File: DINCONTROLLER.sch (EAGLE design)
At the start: 44 parts, among them IC1 ESPWROOM32, SW1 TAC-SWITCH-LEDSP0620, SW2 TAC-SWITCH-LEDSP0620, SW3 TAC-SWITCH-LEDSP0620, SW4 TAC-SWITCH-LEDSP0620, SW5 TAC-SWITCH-LEDSP0620, SW6 TAC-SWITCH-LEDSP0620, SW7 TAC-SWITCH-LEDSP0620, SW8 TAC-SWITCH-LEDSP0620

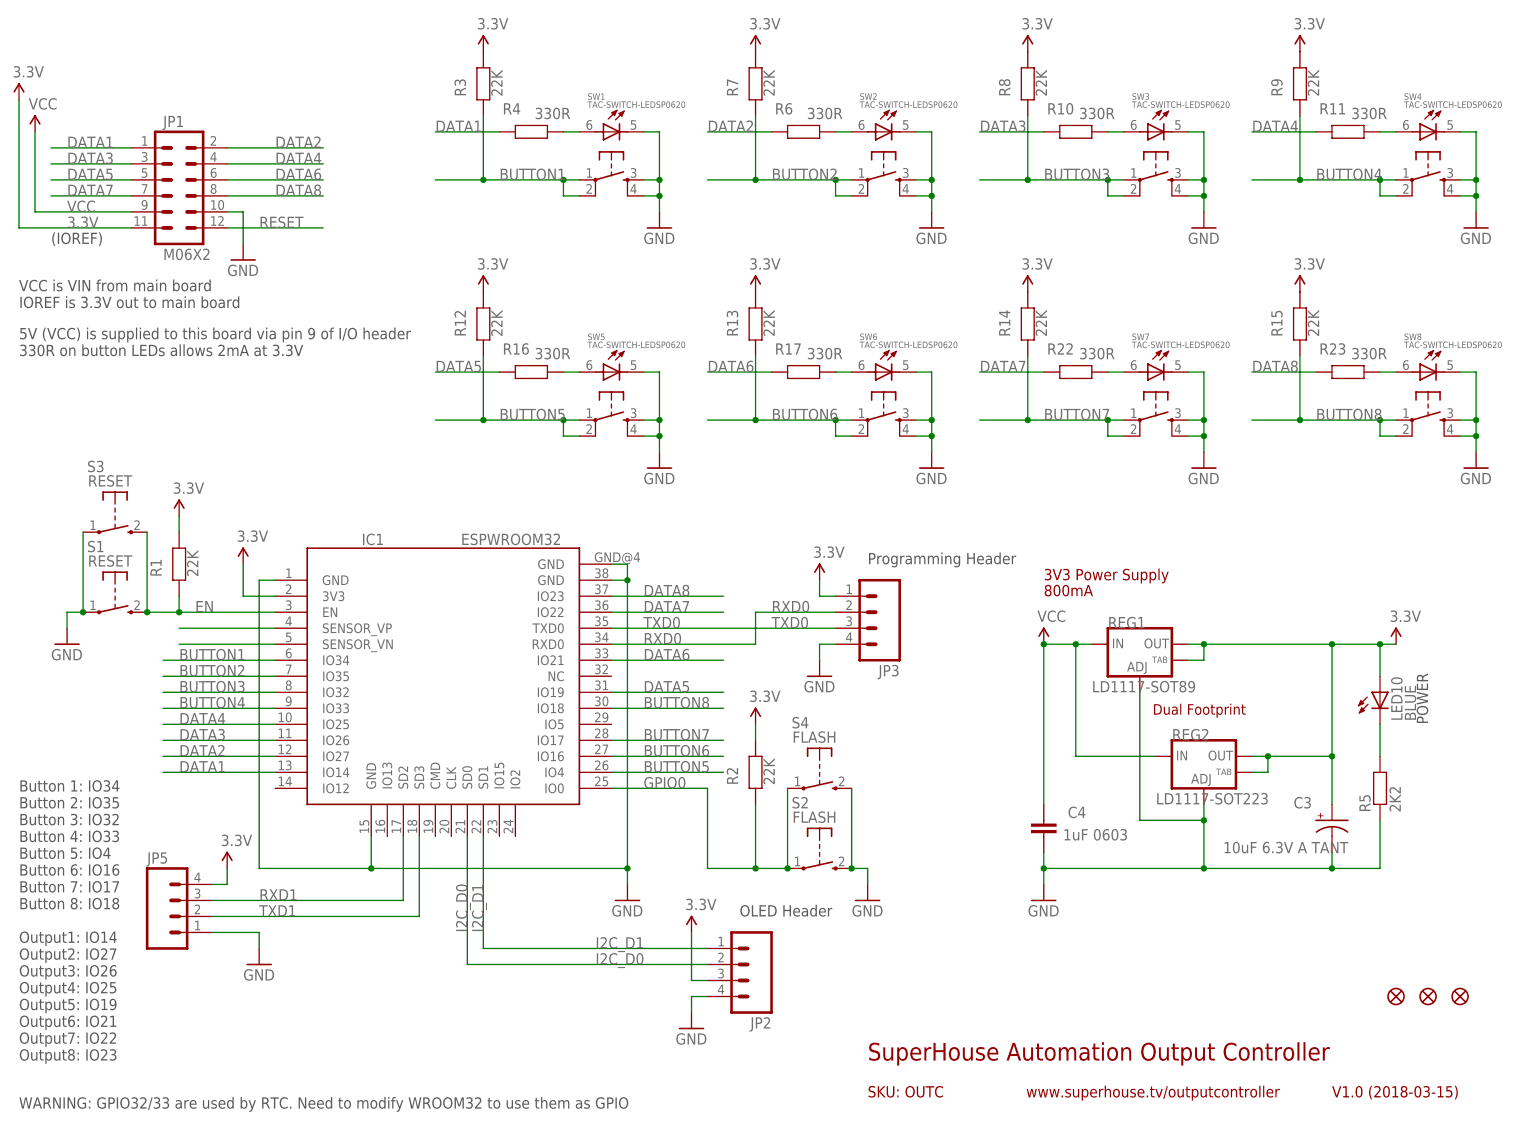
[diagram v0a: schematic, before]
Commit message: Improved designators
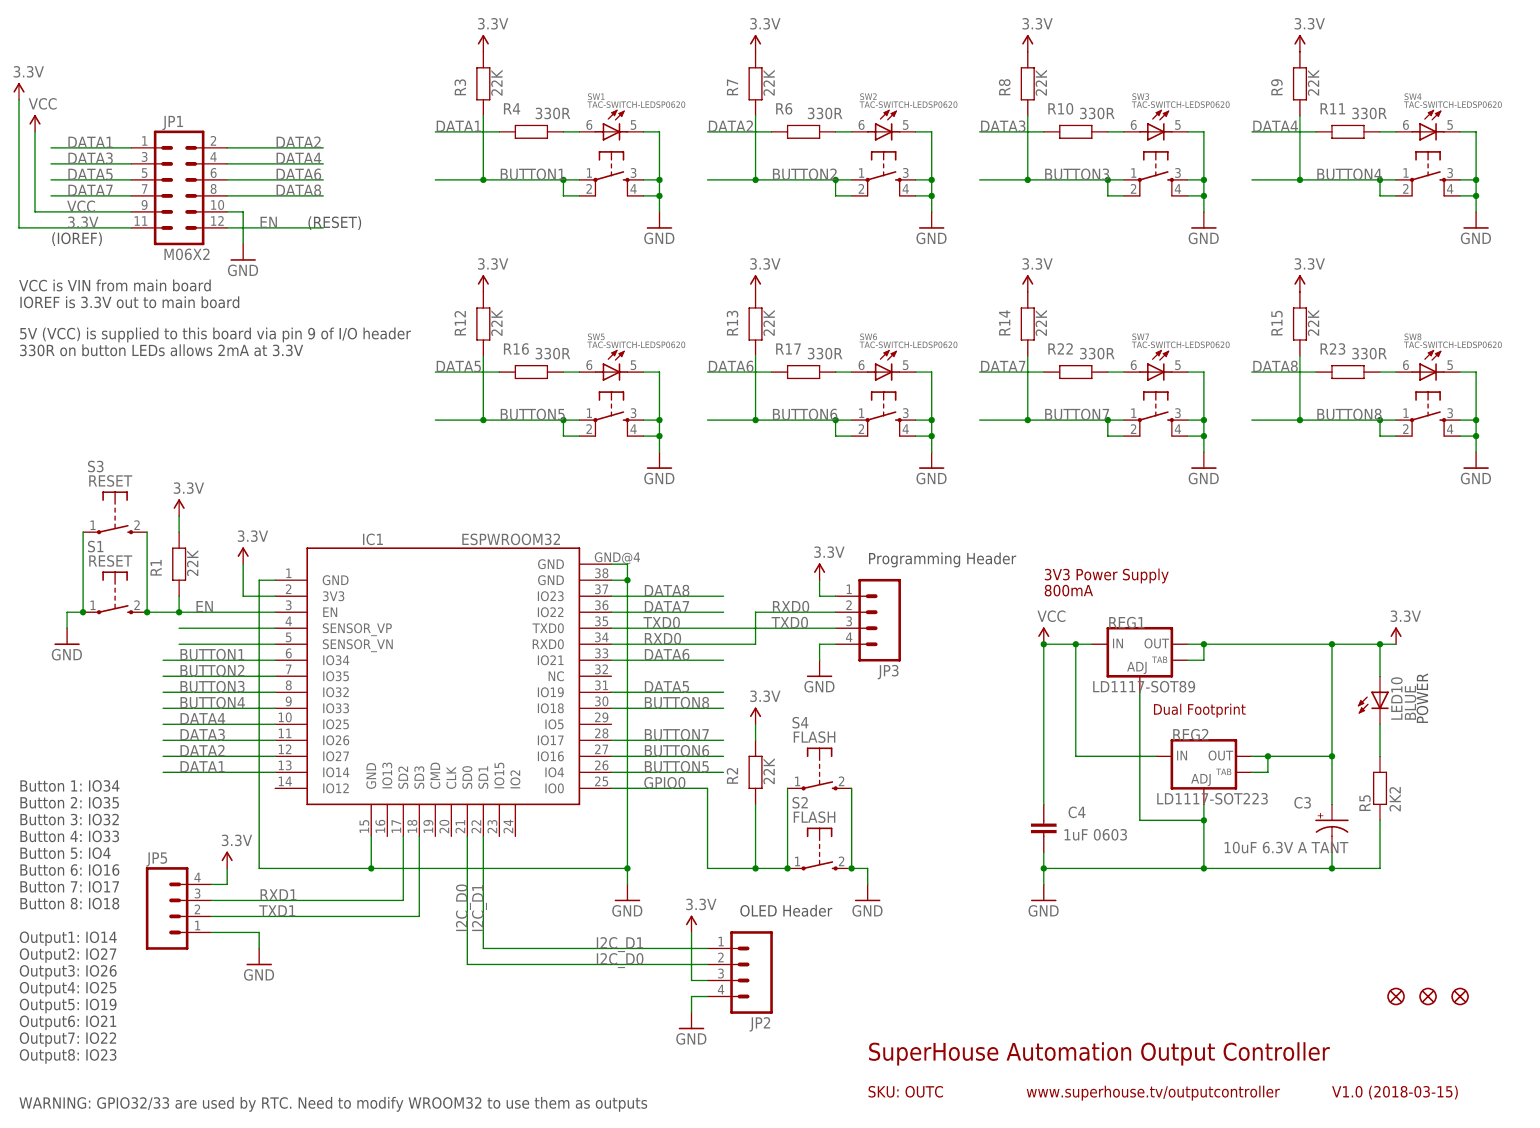
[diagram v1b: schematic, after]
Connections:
- removed net RESET: JP1.12
- net EN: now also JP1.12
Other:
- note added: "(RESET)"
- note added: "WARNING: GPIO32/33 are used by RTC. Need to modify WROOM32 to use them as outputs"
- note removed: "WARNING: GPIO32/33 are used by RTC. Need to modify WROOM32 to use them as GPIO"
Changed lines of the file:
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@@
 <text x="170.18" y="86.36" size="1.778" layer="94">800mA</text>
 <text x="12.7" y="142.24" size="1.778" layer="97">(IOREF)</text>
-<text x="7.62" y="5.08" size="1.778" layer="97">WARNING: GPIO32/33 are used by RTC. Need to modify WROOM32 to use them as GPIO</text>
+<text x="7.62" y="5.08" size="1.778" layer="97">WARNING: GPIO32/33 are used by RTC. Need to modify WROOM32 to use them as outputs</text>
 <text x="121.92" y="35.56" size="1.778" layer="97">OLED Header</text>
 <text x="142.24" y="91.44" size="1.778" layer="97">Programming Header</text>
+<text x="53.34" y="144.78" size="1.778" layer="97">(RESET)</text>
 </plain>
 <instances>
@@
 <label x="33.02" y="66.04" size="1.778" layer="95"/>
 <pinref part="IC1" gate="IC$1" pin="IO25"/>
-</segment>
-</net>
-<net name="RESET" class="0">
-<segment>
-<pinref part="JP1" gate="G$1" pin="12"/>
-<wire x1="40.64" y1="144.78" x2="55.88" y2="144.78" width="0.1524" layer="91"/>
-<label x="45.72" y="144.78" size="1.778" layer="95"/>
 </segment>
 </net>
@@
 <junction x="27.94" y="83.82"/>
 </segment>
+<segment>
+<pinref part="JP1" gate="G$1" pin="12"/>
+<wire x1="40.64" y1="144.78" x2="55.88" y2="144.78" width="0.1524" layer="91"/>
+<label x="45.72" y="144.78" size="1.778" layer="95"/>
+</segment>
 </net>
 <net name="GPIO0" class="0">
@@
 </sheet>
 </sheets>
+<errors>
+</errors>
 </schematic>
 </drawing>

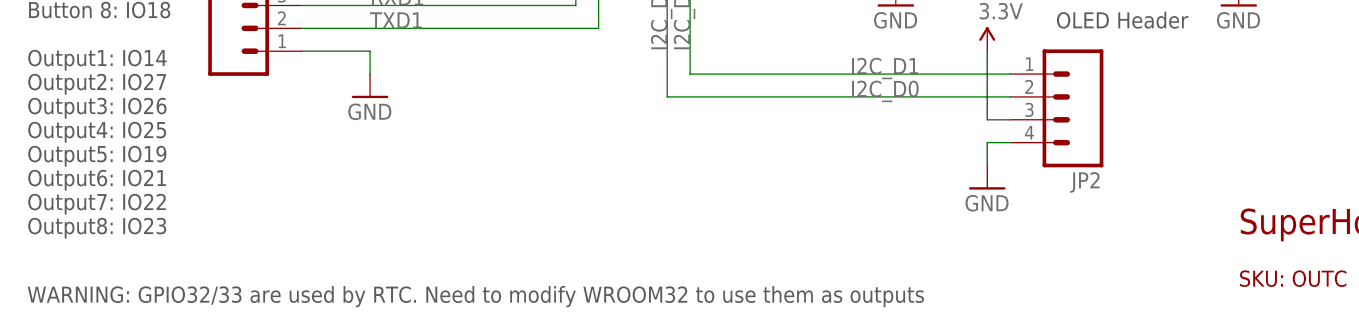
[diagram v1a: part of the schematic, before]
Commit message: Updated notes for v1.0 release
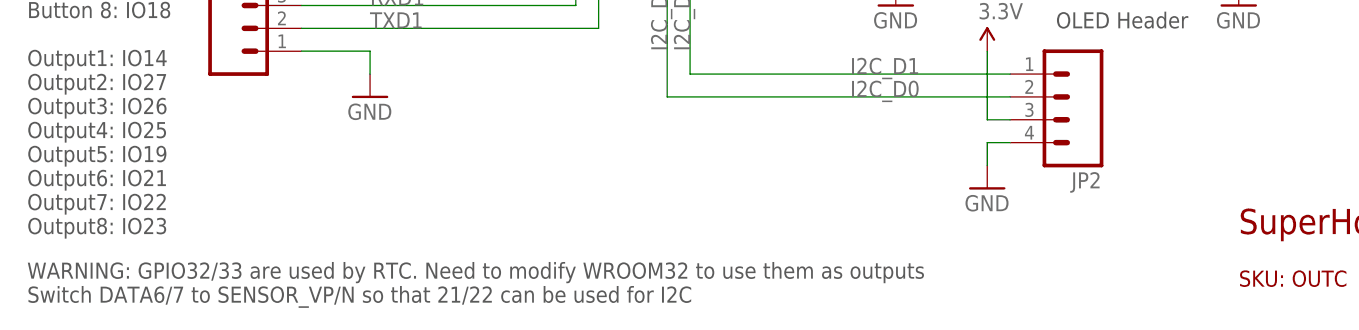
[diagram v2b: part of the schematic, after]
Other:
- note added: "WARNING: GPIO32/33 are used by RTC. Need to modify WROOM32 to use them as outputs Switch DATA6/7 to SENSOR_VP/N so that 21/22 can be used for I2C"
- note removed: "WARNING: GPIO32/33 are used by RTC. Need to modify WROOM32 to use them as outputs"
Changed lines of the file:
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@@
 <?xml version="1.0" encoding="utf-8"?>
 <!DOCTYPE eagle SYSTEM "eagle.dtd">
-<eagle version="8.7.0">
+<eagle version="9.0.0">
 <drawing>
 <settings>
-<setting alwaysvectorfont="no"/>
+<setting alwaysvectorfont="yes"/>
 <setting keepoldvectorfont="yes"/>
 <setting verticaltext="up"/>
@@
 <text x="170.18" y="86.36" size="1.778" layer="94">800mA</text>
 <text x="12.7" y="142.24" size="1.778" layer="97">(IOREF)</text>
-<text x="7.62" y="5.08" size="1.778" layer="97">WARNING: GPIO32/33 are used by RTC. Need to modify WROOM32 to use them as outputs</text>
+<text x="7.62" y="5.08" size="1.778" layer="97">WARNING: GPIO32/33 are used by RTC. Need to modify WROOM32 to use them as outputs
+Switch DATA6/7 to SENSOR_VP/N so that 21/22 can be used for I2C</text>
 <text x="121.92" y="35.56" size="1.778" layer="97">OLED Header</text>
 <text x="142.24" y="91.44" size="1.778" layer="97">Programming Header</text>
